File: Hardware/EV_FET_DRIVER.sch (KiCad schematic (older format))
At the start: 37 parts

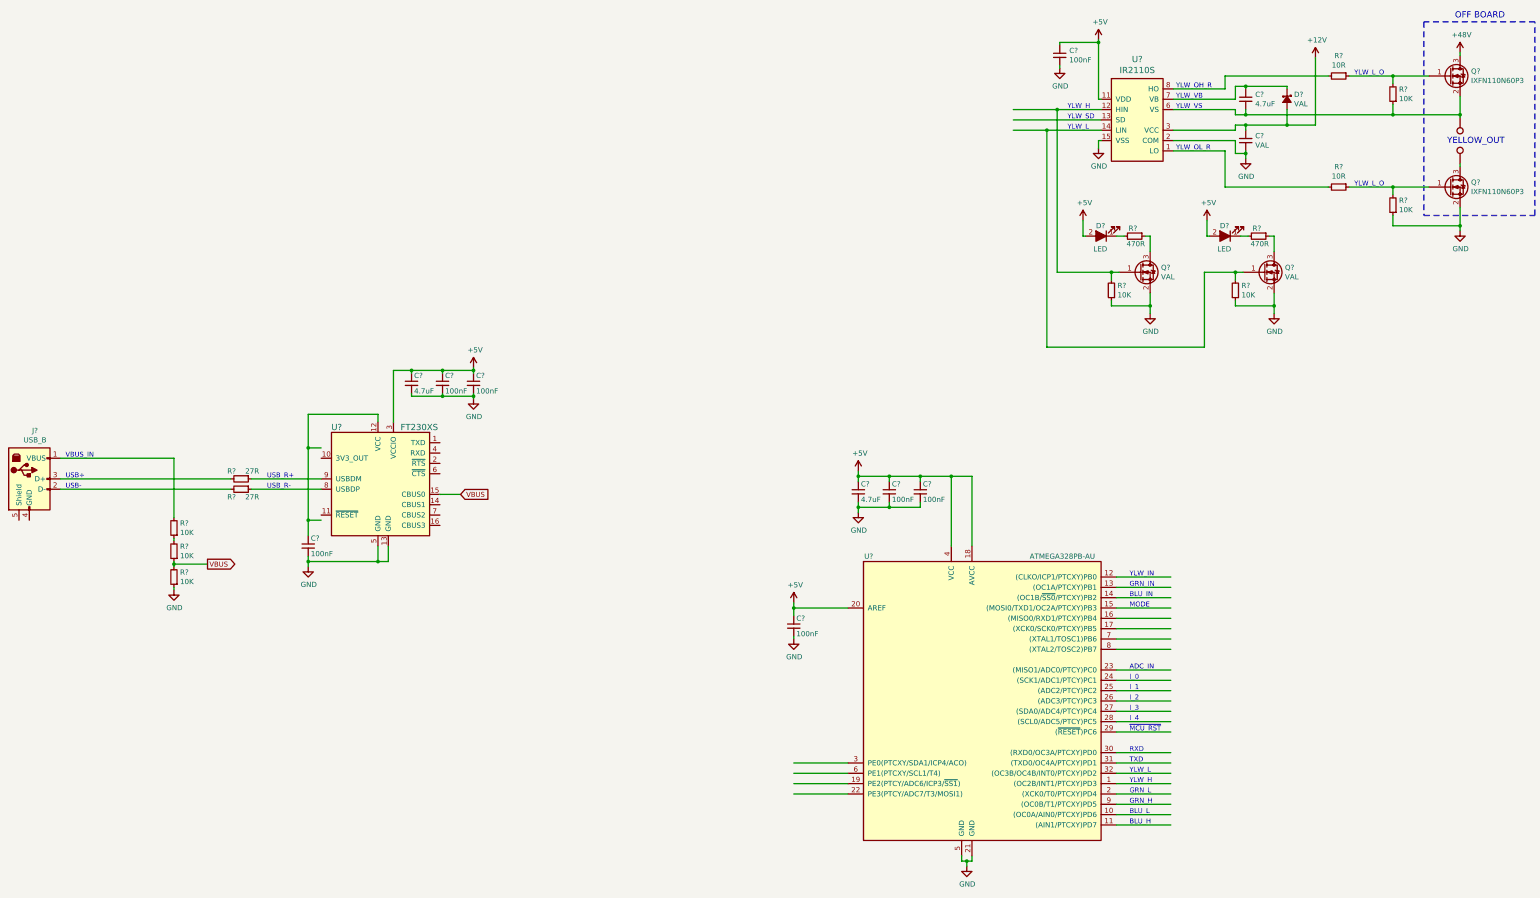
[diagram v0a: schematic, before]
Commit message: Added datasheets. Selected oscillator
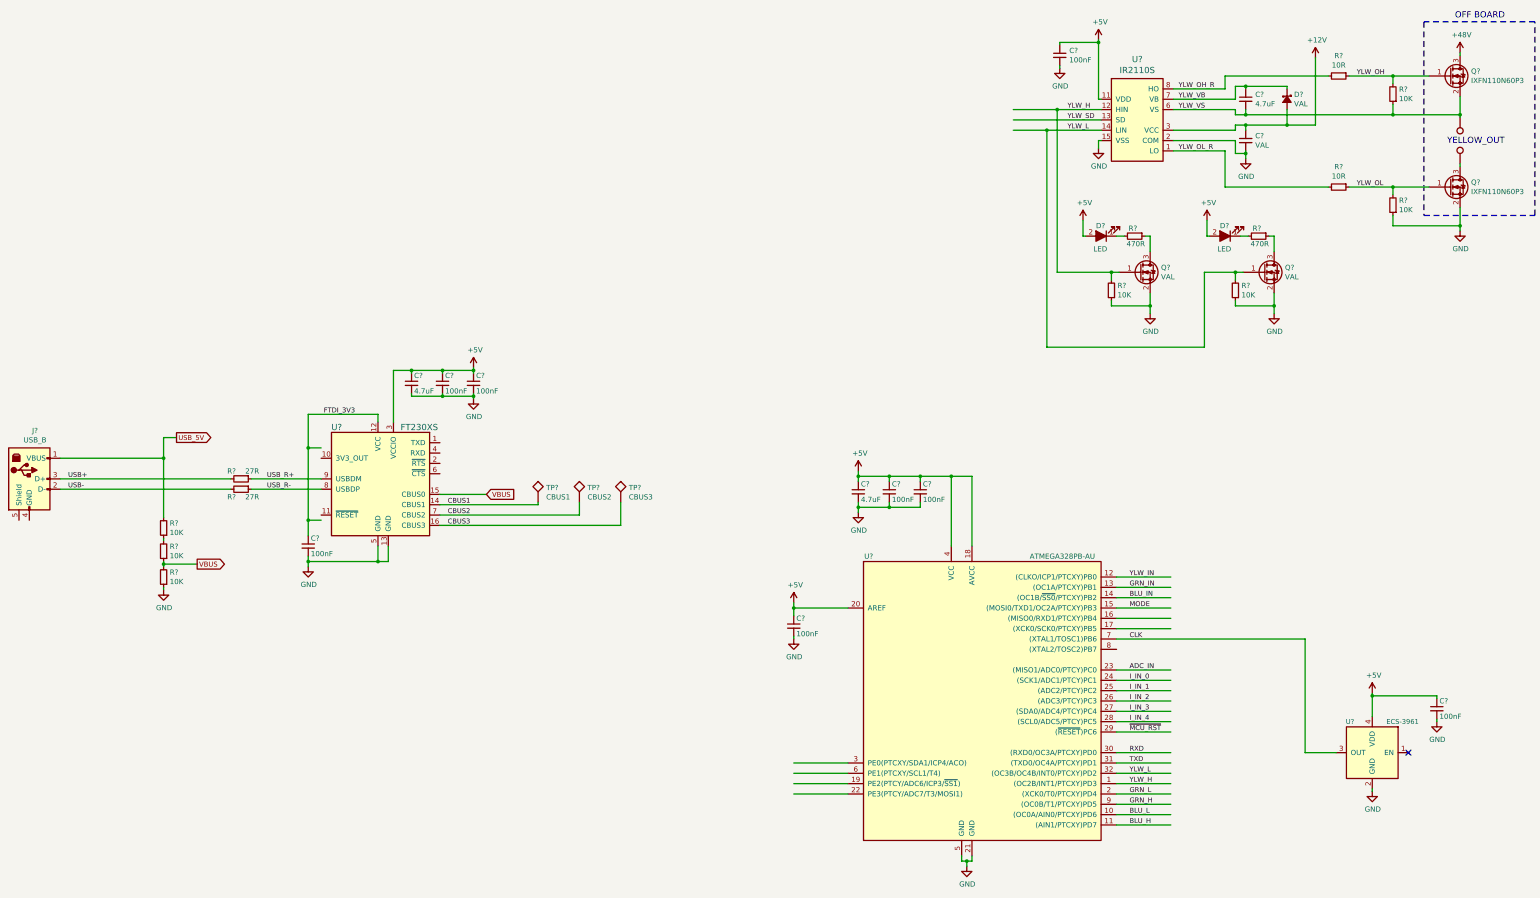
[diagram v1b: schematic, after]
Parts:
- added C?: 100nF, symbol C_Small
- added TP?: CBUS1, symbol TEST
- added TP?: CBUS2, symbol TEST
- added TP?: CBUS3, symbol TEST
- added U?: ECS-3961, symbol ECS-3961
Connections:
- net labels added: ADC_IN, BLU_H, BLU_IN, BLU_L, CBUS1, CBUS2, CBUS3, CLK, FTDI_3V3, GRN_H, GRN_IN, GRN_L, I_IN_0, I_IN_1, I_IN_2, I_IN_3, I_IN_4, MODE, RXD, TXD, USB+, USB-, USB_5V, USB_R+, USB_R-, YLW_H, YLW_IN, YLW_L, YLW_OH, YLW_OH_R, YLW_OL, YLW_OL_R, YLW_SD, YLW_VB, YLW_VS, ~MCU_RST
- wire segments 179 -> 194
- no-connect marks 0 -> 1
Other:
- note removed: "ADC_IN"
- note removed: "BLU_H"
- note removed: "BLU_IN"
- note removed: "BLU_L"
- note removed: "GRN_H"
- note removed: "GRN_IN"
- note removed: "GRN_L"
- note removed: "I_0"
- note removed: "I_1"
- note removed: "I_2"
- note removed: "I_3"
- note removed: "I_4"
- note removed: "MODE"
- note removed: "RXD"
- note removed: "TXD"
- note removed: "USB+"
- note removed: "USB-"
- note removed: "USB_R+"
- note removed: "USB_R-"
- note removed: "VBUS_IN"
- note removed: "YLW_H"
- note removed: "YLW_IN"
- note removed: "YLW_L"
- note removed: "YLW_L_O"
- note removed: "YLW_OH_R"
- note removed: "YLW_OL_R"
- note removed: "YLW_SD"
- note removed: "YLW_VB"
- note removed: "YLW_VS"
- note removed: "~MCU_RST"
- moved on the sheet: R?

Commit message: Added wire
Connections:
- wire segments 194 -> 195
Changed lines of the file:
@@
 Text Label 12000 7125 0    47   ~ 0
 CLK
+Wire Wire Line
+	12400 7225 11875 7225
 $EndSCHEMATC

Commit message: Hardware architecture done. Starting schematic drafting
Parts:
- removed C?: VAL, symbol C_Small
- added C? (x2): 4.7uF, symbol C_Small
- added C? (x10): 100nF, symbol C_Small
- added C? (x3): VAL, symbol CP1_Small
- added C?: VAL, symbol C_Small
- added D? (x2): VAL, symbol D_Schottky_Small_ALT
- added D?: LED_Dual, symbol LED_Dual
- added J?: POWER, symbol CONN_01X02
- added L?: VAL, symbol L_Small
- added R? (x11): VAL, symbol R_Small
- added R?: 10k, symbol R_Small
- added U?: LMR16010, symbol LMR16010
- added U?: TPS22810, symbol TPS22810
- added U?: MCP6561, symbol MCP6561
- added U?: SN74LVC1G04-Q1, symbol SN74LVC1G04-Q1
- U?: symbol FT230XS -> FT230XS-RESCUE-EV_FET_DRIVER
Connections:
- net labels added: +12V_HLDP, +3V3_FTDI, +5V_BUCK, +5V_USB, 12V_PROT, 12V_SEN, AREF, BUCK_B, BUCK_FB, BUCK_SW, CMD_CURR0, CMD_CURR1, CMD_CURR2, CMD_CURR3, CMD_CURR4, DRV_SHDN, GATE_DRV, GLED, I2C, I2C_SCL, I2C_SDA, LINK_CURR, MCU_EXT_INPUTS, PGOOD, POS_A, POS_B, POS_C, UART, VBUS_DET, YLED, YLW_DRVH, YLW_DRVH_R, YLW_DRVL, YLW_DRVL_R
- net labels removed: ADC_IN, BLU_IN, FTDI_3V3, GRN_IN, I_IN_0, I_IN_1, I_IN_2, I_IN_3, I_IN_4, USB_5V, VBUS, YLW_IN, YLW_OH, YLW_OH_R, YLW_OL, YLW_OL_R, YLW_SD
- wire segments 195 -> 331
- no-connect marks 1 -> 3
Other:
- moved on the sheet: C?, D?, Q?, R?, TP?, U?
